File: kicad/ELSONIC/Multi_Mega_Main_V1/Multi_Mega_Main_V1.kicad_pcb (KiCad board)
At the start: 2 copper layers, 5 parts, among them U1 STM32G474METx, Y1 HC-49SMD

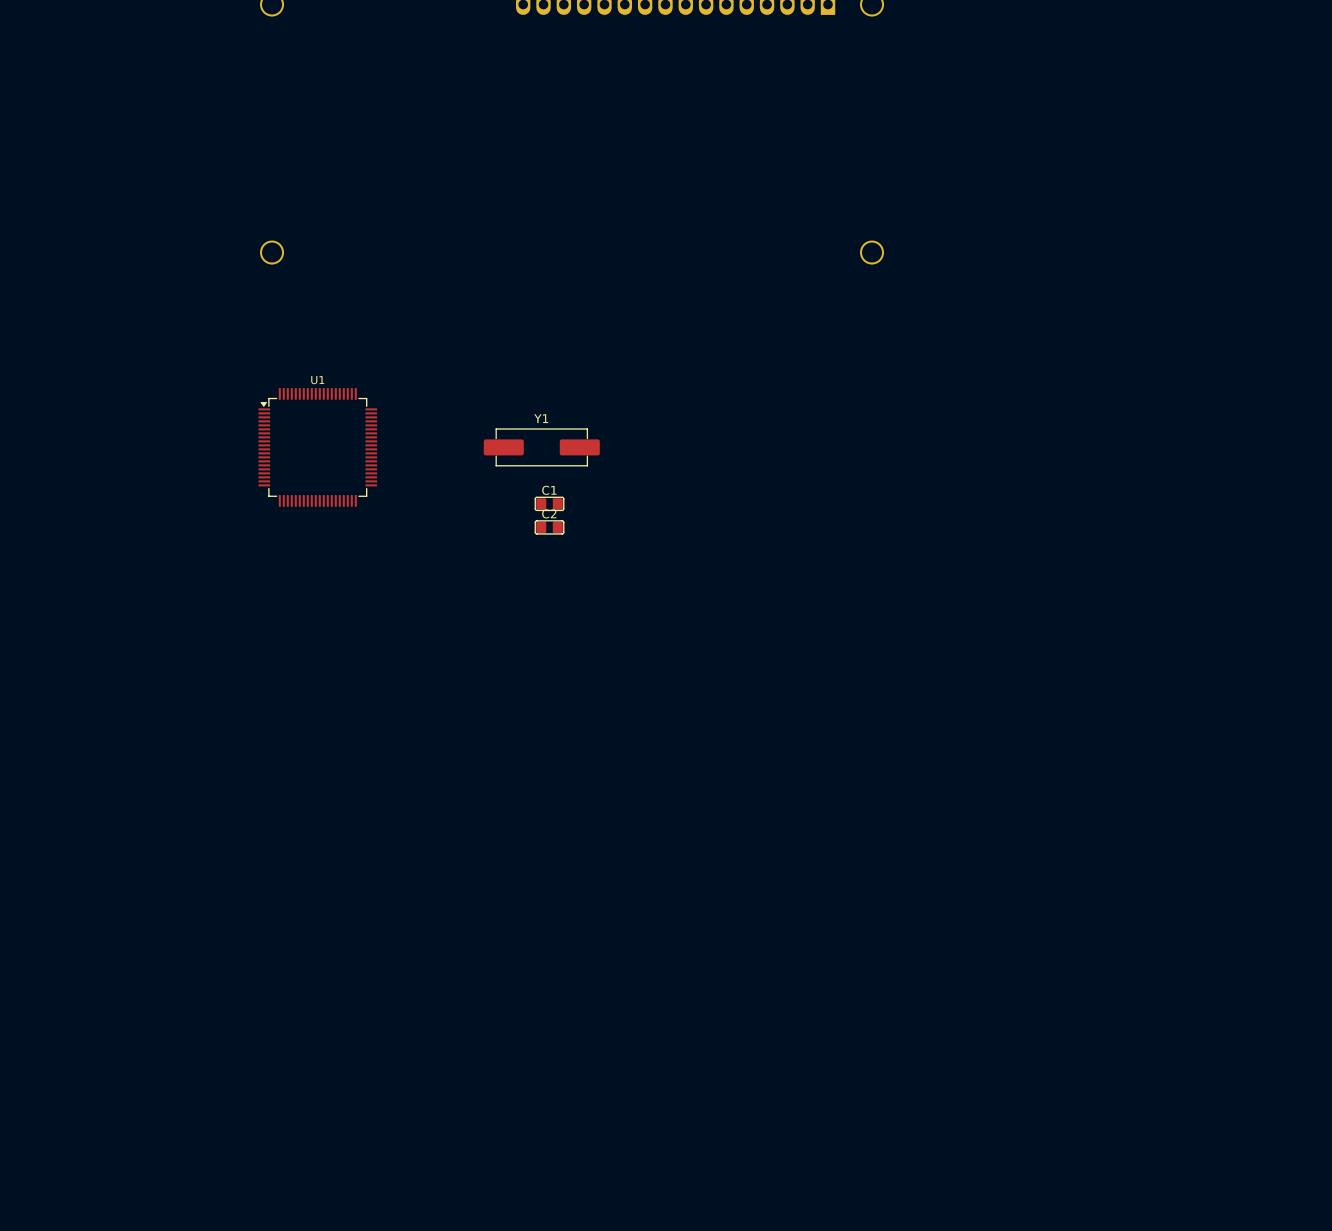
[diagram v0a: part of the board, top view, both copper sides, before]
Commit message: 회로도 구성 완료
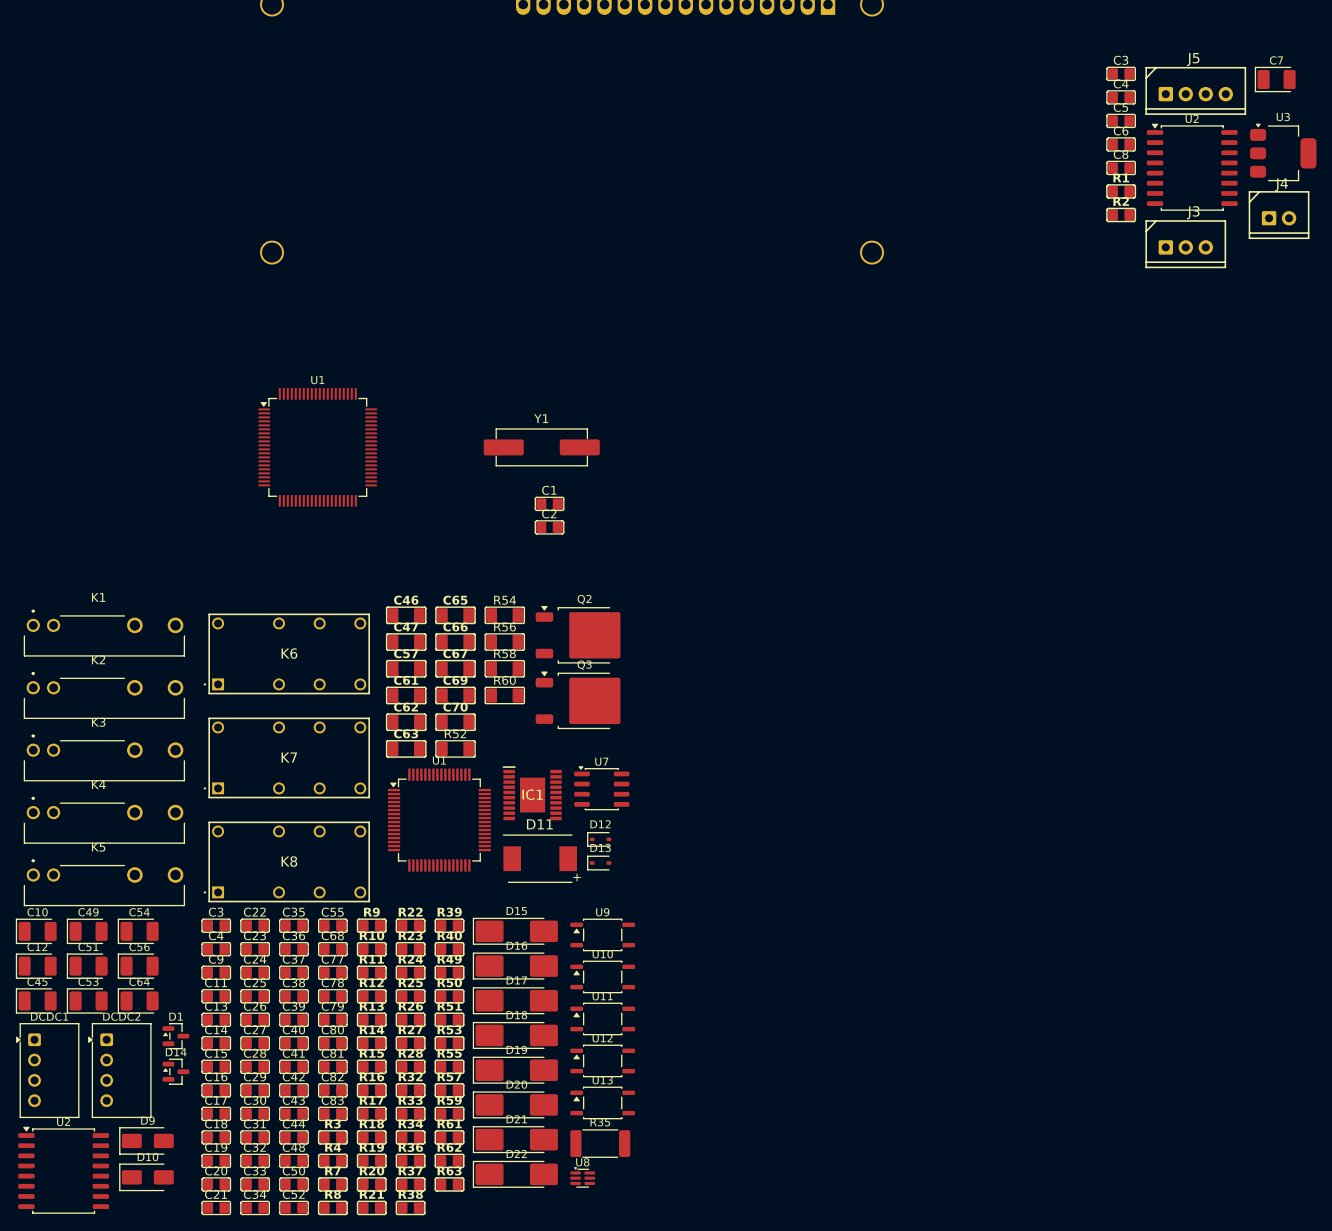
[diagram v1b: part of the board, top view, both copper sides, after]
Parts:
- added C10: 47UF50V, 04_MyFoot_Passive:CP_EIA-3528-21_Kemet-B_HandSolder, F.Cu at (46.0, 157.5)
- added C11: CL104K, 04_MyFoot_Passive:C_2012Metric, F.Cu at (68.3, 165.6)
- added C12: 10UF25V, 04_MyFoot_Passive:CP_EIA-3528-21_Kemet-B_HandSolder, F.Cu at (46.0, 161.8)
- added C13: CL104K, 04_MyFoot_Passive:C_2012Metric, F.Cu at (68.3, 168.6)
- added C14: CL475K, 04_MyFoot_Passive:C_2012Metric, F.Cu at (68.3, 171.5)
- added C15: CL104K, 04_MyFoot_Passive:C_2012Metric, F.Cu at (68.3, 174.4)
- added C16: CL104K, 04_MyFoot_Passive:C_2012Metric, F.Cu at (68.3, 177.4)
- added C17: CL105K, 04_MyFoot_Passive:C_2012Metric, F.Cu at (68.3, 180.3)
- added C18: CL104K, 04_MyFoot_Passive:C_2012Metric, F.Cu at (68.3, 183.2)
- added C19: CL104K, 04_MyFoot_Passive:C_2012Metric, F.Cu at (68.3, 186.2)
- added C20: CL104K, 04_MyFoot_Passive:C_2012Metric, F.Cu at (68.3, 189.1)
- added C21: CG101J, 04_MyFoot_Passive:C_2012Metric, F.Cu at (68.3, 192.1)
- added C22: CL104K, 04_MyFoot_Passive:C_2012Metric, F.Cu at (73.2, 156.8)
- added C23: CL104K, 04_MyFoot_Passive:C_2012Metric, F.Cu at (73.2, 159.7)
- added C24: CL104K, 04_MyFoot_Passive:C_2012Metric, F.Cu at (73.2, 162.7)
- added C25: CL104K, 04_MyFoot_Passive:C_2012Metric, F.Cu at (73.2, 165.6)
- added C26: CL104K, 04_MyFoot_Passive:C_2012Metric, F.Cu at (73.2, 168.6)
- added C27: CL104K, 04_MyFoot_Passive:C_2012Metric, F.Cu at (73.2, 171.5)
- added C28: CL106K, 04_MyFoot_Passive:C_2012Metric, F.Cu at (73.2, 174.4)
- added C29: CL104K, 04_MyFoot_Passive:C_2012Metric, F.Cu at (73.2, 177.4)
- added C3: CL104K, 04_MyFoot_Passive:C_2012Metric, F.Cu at (68.3, 156.8)
- added C3: CG220J, 04_MyFoot_Passive:C_2012Metric, F.Cu at (181.4, 50.3)
- added C30: CL475K, 04_MyFoot_Passive:C_2012Metric, F.Cu at (73.2, 180.3)
- added C31: CL104K, 04_MyFoot_Passive:C_2012Metric, F.Cu at (73.2, 183.2)
- added C32: CL104K, 04_MyFoot_Passive:C_2012Metric, F.Cu at (73.2, 186.2)
- added C33: CL105K, 04_MyFoot_Passive:C_2012Metric, F.Cu at (73.2, 189.1)
- added C34: CL104K, 04_MyFoot_Passive:C_2012Metric, F.Cu at (73.2, 192.1)
- added C35: B472K, 04_MyFoot_Passive:C_2012Metric, F.Cu at (78.0, 156.8)
- added C36: B472K, 04_MyFoot_Passive:C_2012Metric, F.Cu at (78.0, 159.7)
- added C37: CL104K, 04_MyFoot_Passive:C_2012Metric, F.Cu at (78.0, 162.7)
- added C38: CL104K, 04_MyFoot_Passive:C_2012Metric, F.Cu at (78.0, 165.6)
- added C39: CL104K, 04_MyFoot_Passive:C_2012Metric, F.Cu at (78.0, 168.6)
- added C4: CG220J, 04_MyFoot_Passive:C_2012Metric, F.Cu at (181.4, 53.2)
- added C4: CL475K, 04_MyFoot_Passive:C_2012Metric, F.Cu at (68.3, 159.7)
- added C40: CL104K, 04_MyFoot_Passive:C_2012Metric, F.Cu at (78.0, 171.5)
- added C41: CL104K, 04_MyFoot_Passive:C_2012Metric, F.Cu at (78.0, 174.4)
- added C42: CG220J, 04_MyFoot_Passive:C_2012Metric, F.Cu at (78.0, 177.4)
- added C43: CG220J, 04_MyFoot_Passive:C_2012Metric, F.Cu at (78.0, 180.3)
- added C44: CL104K, 04_MyFoot_Passive:C_2012Metric, F.Cu at (78.0, 183.2)
- added C45: TAJB106K, 04_MyFoot_Passive:CP_EIA-3528-21_Kemet-B_HandSolder, F.Cu at (46.0, 166.2)
- added C46: 225J100V, 04_MyFoot_Passive:C_3216Metric, F.Cu at (92.1, 118.0)
- added C47: 225J100V, 04_MyFoot_Passive:C_3216Metric, F.Cu at (92.1, 121.3)
- added C48: CL104K, 04_MyFoot_Passive:C_2012Metric, F.Cu at (78.0, 186.2)
- added C49: 47UF50V, 04_MyFoot_Passive:CP_EIA-3528-21_Kemet-B_HandSolder, F.Cu at (52.4, 157.5)
- added C5: CL104K, 04_MyFoot_Passive:C_2012Metric, F.Cu at (181.4, 56.2)
- added C50: CL104K, 04_MyFoot_Passive:C_2012Metric, F.Cu at (78.0, 189.1)
- added C51: 10UF25V, 04_MyFoot_Passive:CP_EIA-3528-21_Kemet-B_HandSolder, F.Cu at (52.4, 161.8)
- added C52: 104KC100V, 04_MyFoot_Passive:C_2012Metric, F.Cu at (78.0, 192.1)
- added C53: 10UF100V, 04_MyFoot_Passive:CP_EIA-3528-21_Kemet-B_HandSolder, F.Cu at (52.4, 166.2)
- added C54: 1000UF63V, 04_MyFoot_Passive:CP_EIA-3528-21_Kemet-B_HandSolder, F.Cu at (58.7, 157.5)
- added C55: CL104K, 04_MyFoot_Passive:C_2012Metric, F.Cu at (82.9, 156.8)
- added C56: TAJB106K, 04_MyFoot_Passive:CP_EIA-3528-21_Kemet-B_HandSolder, F.Cu at (58.7, 161.8)
- added C57: 105J100V, 04_MyFoot_Passive:C_3216Metric, F.Cu at (92.1, 124.7)
- added C6: CL104K, 04_MyFoot_Passive:C_2012Metric, F.Cu at (181.4, 59.1)
- added C61: 102J100V, 04_MyFoot_Passive:C_3216Metric, F.Cu at (92.1, 128.0)
- added C62: 223J100V, 04_MyFoot_Passive:C_3216Metric, F.Cu at (92.1, 131.3)
- added C63: 330J100V, 04_MyFoot_Passive:C_3216Metric, F.Cu at (92.1, 134.7)
- added C64: 220UF50V, 04_MyFoot_Passive:CP_EIA-3528-21_Kemet-B_HandSolder, F.Cu at (58.7, 166.2)
- added C65: 330J100V, 04_MyFoot_Passive:C_3216Metric, F.Cu at (98.2, 118.0)
- added C66: 103J100V, 04_MyFoot_Passive:C_3216Metric, F.Cu at (98.2, 121.3)
- added C67: 226J50V, 04_MyFoot_Passive:C_3216Metric, F.Cu at (98.2, 124.7)
- added C68: CL104K, 04_MyFoot_Passive:C_2012Metric, F.Cu at (82.9, 159.7)
- added C69: 103J100V, 04_MyFoot_Passive:C_3216Metric, F.Cu at (98.2, 128.0)
- added C7: TAJB106K, 04_MyFoot_Passive:CP_EIA-3528-21_Kemet-B_HandSolder, F.Cu at (200.9, 51.0)
- added C70: 101J100V, 04_MyFoot_Passive:C_3216Metric, F.Cu at (98.2, 131.3)
- added C77: B472K, 04_MyFoot_Passive:C_2012Metric, F.Cu at (82.9, 162.7)
- added C78: B472K, 04_MyFoot_Passive:C_2012Metric, F.Cu at (82.9, 165.6)
- added C79: B472K, 04_MyFoot_Passive:C_2012Metric, F.Cu at (82.9, 168.6)
- added C8: CL106K, 04_MyFoot_Passive:C_2012Metric, F.Cu at (181.4, 62.1)
- added C80: CL106K, 04_MyFoot_Passive:C_2012Metric, F.Cu at (82.9, 171.5)
- added C81: CL104K, 04_MyFoot_Passive:C_2012Metric, F.Cu at (82.9, 174.4)
- added C82: CL106K, 04_MyFoot_Passive:C_2012Metric, F.Cu at (82.9, 177.4)
- added C83: CL104K, 04_MyFoot_Passive:C_2012Metric, F.Cu at (82.9, 180.3)
- added C9: CL104K, 04_MyFoot_Passive:C_2012Metric, F.Cu at (68.3, 162.7)
- added D1: BAV99, Package_TO_SOT_SMD:SOT-23, F.Cu at (63.3, 170.6)
- added D10: SS24, Diode_SMD:D_SMA, F.Cu at (59.8, 188.2)
- added D11: B3100-13-F, 03_MyFoot_Active:B3100_13_F, F.Cu at (108.8, 148.4)
- added D12: BAT54WS, Diode_SMD:D_SOD-323, F.Cu at (116.3, 146.0)
- added D13: BAT54WS, Diode_SMD:D_SOD-323, F.Cu at (116.3, 149.0)
- added D14: SM712_SOT23, Package_TO_SOT_SMD:SOT-23, F.Cu at (63.3, 175.0)
- added D15: LL4148, 03_MyFoot_Active:D_MELF_Hand, F.Cu at (105.9, 157.5)
- added D16: LL4148, 03_MyFoot_Active:D_MELF_Hand, F.Cu at (105.9, 161.8)
- added D17: LL4148, 03_MyFoot_Active:D_MELF_Hand, F.Cu at (105.9, 166.2)
- added D18: LL4148, 03_MyFoot_Active:D_MELF_Hand, F.Cu at (105.9, 170.5)
- added D19: LL4148, 03_MyFoot_Active:D_MELF_Hand, F.Cu at (105.9, 174.8)
- added D20: LL4148, 03_MyFoot_Active:D_MELF_Hand, F.Cu at (105.9, 179.2)
- added D21: LL4148, 03_MyFoot_Active:D_MELF_Hand, F.Cu at (105.9, 183.5)
- added D22: LL4148, 03_MyFoot_Active:D_MELF_Hand, F.Cu at (105.9, 187.9)
- added D9: SS24, Diode_SMD:D_SMA, F.Cu at (59.8, 183.7)
- added DCDC1: MUS2415N, Converter_DCDC:Converter_DCDC_TRACO_TME_24xxS_Single_THT, F.Cu at (45.6, 171.0)
- added DCDC2: MUS2415N, Converter_DCDC:Converter_DCDC_TRACO_TME_24xxS_Single_THT, F.Cu at (54.6, 171.0)
- added IC1: LM5005MHX_NOPB, 01_MyFoot_ICs:SOP65P640X110-21N, F.Cu at (107.9, 140.5)
- added J3: SMW250-03P, 02_MyFoot_Connectors:SMW250_03P, F.Cu at (189.5, 72.0)
- added J4: SMW250-02P, 02_MyFoot_Connectors:SMW250_02P, F.Cu at (201.2, 68.4)
- added J5: SMW250-04P, 02_MyFoot_Connectors:SMW250_04P, F.Cu at (190.8, 52.8)
- added K1: PA1A_5V, 06_MyFoot_Mechanical:PA1A5V, F.Cu at (45.4, 119.2)
- added K2: PA1A_5V, 06_MyFoot_Mechanical:PA1A5V, F.Cu at (45.4, 127.0)
- added K3: PA1A_5V, 06_MyFoot_Mechanical:PA1A5V, F.Cu at (45.4, 134.8)
- added K4: PA1A_5V, 06_MyFoot_Mechanical:PA1A5V, F.Cu at (45.4, 142.7)
- added K5: PA1A_5V, 06_MyFoot_Mechanical:PA1A5V, F.Cu at (45.4, 150.4)
- added K6: G6A274, 06_MyFoot_Mechanical:G6A274PST15USDC12, F.Cu at (68.5, 126.6)
- added K7: G6A274, 06_MyFoot_Mechanical:G6A274PST15USDC12, F.Cu at (68.5, 139.6)
- added K8: G6A274, 06_MyFoot_Mechanical:G6A274PST15USDC12, F.Cu at (68.5, 152.6)
- added Q2: STD25N10F7, Package_TO_SOT_SMD:TO-252-2, F.Cu at (114.4, 120.5)
- added Q3: STD25N10F7, Package_TO_SOT_SMD:TO-252-2, F.Cu at (114.4, 128.7)
- added R1: FR-0747RL, 04_MyFoot_Passive:R_2012Metric, F.Cu at (181.4, 65.0)
- added R10: W8-J0561, 04_MyFoot_Passive:R_2012Metric, F.Cu at (87.7, 159.7)
- added R11: W8-J0561, 04_MyFoot_Passive:R_2012Metric, F.Cu at (87.7, 162.7)
- added R12: W8-J0561, 04_MyFoot_Passive:R_2012Metric, F.Cu at (87.7, 165.6)
- added R13: W8-J0561, 04_MyFoot_Passive:R_2012Metric, F.Cu at (87.7, 168.6)
- added R14: W8-J0103, 04_MyFoot_Passive:R_2012Metric, F.Cu at (87.7, 171.5)
- added R15: W8-J0103, 04_MyFoot_Passive:R_2012Metric, F.Cu at (87.7, 174.4)
- added R16: W8-J0103, 04_MyFoot_Passive:R_2012Metric, F.Cu at (87.7, 177.4)
- added R17: W8-J0103, 04_MyFoot_Passive:R_2012Metric, F.Cu at (87.7, 180.3)
- added R18: W8-J0103, 04_MyFoot_Passive:R_2012Metric, F.Cu at (87.7, 183.2)
- added R19: W4-J0220, 04_MyFoot_Passive:R_2012Metric, F.Cu at (87.7, 186.2)
- added R2: FR-0747RL, 04_MyFoot_Passive:R_2012Metric, F.Cu at (181.4, 68.0)
- added R20: W8-J0103, 04_MyFoot_Passive:R_2012Metric, F.Cu at (87.7, 189.1)
- added R21: W8-J0104, 04_MyFoot_Passive:R_2012Metric, F.Cu at (87.7, 192.1)
- added R22: W4-J0103, 04_MyFoot_Passive:R_2012Metric, F.Cu at (92.6, 156.8)
- added R23: 1W-4.7, 04_MyFoot_Passive:R_2012Metric, F.Cu at (92.6, 159.7)
- added R24: 1W-4.7, 04_MyFoot_Passive:R_2012Metric, F.Cu at (92.6, 162.7)
- added R25: W4-J0103, 04_MyFoot_Passive:R_2012Metric, F.Cu at (92.6, 165.6)
- added R26: W4-J0334, 04_MyFoot_Passive:R_2012Metric, F.Cu at (92.6, 168.6)
- added R27: W4-F4992, 04_MyFoot_Passive:R_2012Metric, F.Cu at (92.6, 171.5)
- added R28: W4-J0333, 04_MyFoot_Passive:R_2012Metric, F.Cu at (92.6, 174.4)
- added R3: W8-J0103, 04_MyFoot_Passive:R_2012Metric, F.Cu at (82.9, 183.2)
- added R32: W4-F1102, 04_MyFoot_Passive:R_2012Metric, F.Cu at (92.6, 177.4)
- added R33: W4-F1501, 04_MyFoot_Passive:R_2012Metric, F.Cu at (92.6, 180.3)
- added R34: W4-F2701, 04_MyFoot_Passive:R_2012Metric, F.Cu at (92.6, 183.2)
- added R35: 1W-F100, Resistor_SMD:R_2512_6332Metric_Pad1.40x3.35mm_HandSolder, F.Cu at (116.3, 184.0)
- added R36: W4-J0100, 04_MyFoot_Passive:R_2012Metric, F.Cu at (92.6, 186.2)
- added R37: W4-J0123, 04_MyFoot_Passive:R_2012Metric, F.Cu at (92.6, 189.1)
- added R38: W4-J0223, 04_MyFoot_Passive:R_2012Metric, F.Cu at (92.6, 192.1)
- added R39: W4-F1102, 04_MyFoot_Passive:R_2012Metric, F.Cu at (97.5, 156.8)
- added R4: W4-J0470, 04_MyFoot_Passive:R_2012Metric, F.Cu at (82.9, 186.2)
- added R40: W4-F1501, 04_MyFoot_Passive:R_2012Metric, F.Cu at (97.5, 159.7)
- added R49: W8-J0431, 04_MyFoot_Passive:R_2012Metric, F.Cu at (97.5, 162.7)
- added R50: W8-J0431, 04_MyFoot_Passive:R_2012Metric, F.Cu at (97.5, 165.6)
- added R51: W4-J0121, 04_MyFoot_Passive:R_2012Metric, F.Cu at (97.5, 168.6)
- added R52: W4-J0472, 04_MyFoot_Passive:R_3216Metric, F.Cu at (98.2, 134.7)
- added R53: W8-J0103, 04_MyFoot_Passive:R_2012Metric, F.Cu at (97.5, 171.5)
- added R54: W4-J0472, 04_MyFoot_Passive:R_3216Metric, F.Cu at (104.4, 118.0)
- added R55: W8-J0103, 04_MyFoot_Passive:R_2012Metric, F.Cu at (97.5, 174.4)
- added R56: W4-J0472, 04_MyFoot_Passive:R_3216Metric, F.Cu at (104.4, 121.3)
- added R57: W8-J0103, 04_MyFoot_Passive:R_2012Metric, F.Cu at (97.5, 177.4)
- added R58: W4-J0472, 04_MyFoot_Passive:R_3216Metric, F.Cu at (104.4, 124.7)
- added R59: W8-J0103, 04_MyFoot_Passive:R_2012Metric, F.Cu at (97.5, 180.3)
- added R60: W4-J0472, 04_MyFoot_Passive:R_3216Metric, F.Cu at (104.4, 128.0)
- added R61: W8-J0103, 04_MyFoot_Passive:R_2012Metric, F.Cu at (97.5, 183.2)
- added R62: FR-0733RL, 04_MyFoot_Passive:R_2012Metric, F.Cu at (97.5, 186.2)
- added R63: W8-J0103, 04_MyFoot_Passive:R_2012Metric, F.Cu at (97.5, 189.1)
- added R7: W8-J0103, 04_MyFoot_Passive:R_2012Metric, F.Cu at (82.9, 189.1)
- added R8: W8-J0561, 04_MyFoot_Passive:R_2012Metric, F.Cu at (82.9, 192.1)
- added R9: W8-J0561, 04_MyFoot_Passive:R_2012Metric, F.Cu at (87.7, 156.8)
- added U1: STM32G474RBT6, Package_QFP:LQFP-64_10x10mm_P0.5mm, F.Cu at (96.2, 143.6)
- added U10: TLP185, 01_MyFoot_ICs:SOIC-4_4.55x3.7mm_P2.54mm, F.Cu at (116.6, 163.2)
- added U11: TLP185, 01_MyFoot_ICs:SOIC-4_4.55x3.7mm_P2.54mm, F.Cu at (116.6, 168.4)
- added U12: TLP185, 01_MyFoot_ICs:SOIC-4_4.55x3.7mm_P2.54mm, F.Cu at (116.6, 173.7)
- added U13: TLP185, 01_MyFoot_ICs:SOIC-4_4.55x3.7mm_P2.54mm, F.Cu at (116.6, 178.9)
- added U2: UCC21520DW, Package_SO:SOIC-16W_7.5x10.3mm_P1.27mm, F.Cu at (49.2, 187.5)
- added U2: UCC21520DW, Package_SO:SOIC-16W_7.5x10.3mm_P1.27mm, F.Cu at (190.3, 62.1)
- added U3: AMS1117-3.3, Package_TO_SOT_SMD:SOT-223-3_TabPin2, F.Cu at (201.7, 60.2)
- added U7: MAX3485, Package_SO:SOIC-8_3.9x4.9mm_P1.27mm, F.Cu at (116.5, 139.7)
- added U8: INA190A4, Package_TO_SOT_SMD:SOT-363_SC-70-6, F.Cu at (114.1, 188.3)
- added U9: TLP185, 01_MyFoot_ICs:SOIC-4_4.55x3.7mm_P2.54mm, F.Cu at (116.6, 157.9)
- LCD1: renamed from DS1; value WC1602A -> LC1602A
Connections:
- LCD1 pad 1: unconnected-(DS1-VSS-Pad1) -> GND
- LCD1 pad 11: unconnected-(DS1-D4-Pad11) -> Net-(LCD1-D4)
- LCD1 pad 12: unconnected-(DS1-D5-Pad12) -> Net-(LCD1-D5)
- LCD1 pad 13: unconnected-(DS1-D6-Pad13) -> Net-(LCD1-D6)
- LCD1 pad 14: unconnected-(DS1-D7-Pad14) -> Net-(LCD1-D7)
- LCD1 pad 15: unconnected-(DS1-LED(+)-Pad15) -> Net-(LCD1-LED(+))
- LCD1 pad 16: unconnected-(DS1-LED(-)-Pad16) -> GND
- LCD1 pad 2: unconnected-(DS1-VDD-Pad2) -> +5V
- LCD1 pad 3: unconnected-(DS1-VO-Pad3) -> Net-(LCD1-VO)
- LCD1 pad 4: unconnected-(DS1-RS-Pad4) -> Net-(LCD1-RS)
- LCD1 pad 5: unconnected-(DS1-R/W-Pad5) -> GND
- LCD1 pad 6: unconnected-(DS1-E-Pad6) -> Net-(LCD1-E)
- U1 pad 56: unconnected-(U1-PA8-Pad56) -> Net-(U1-PA8)
- U1 pad 57: unconnected-(U1-PA9-Pad57) -> Net-(U1-PA9)

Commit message: chore: KiCad 아트웍 및 라이브러리 변경 반영
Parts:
- removed the U1 at (81.0, 97.0)
- added D23: LL4148, 03_MyFoot_Active:D_MELF_Hand, F.Cu at (111.5, -91.5)
- added K9: G6A274, 06_MyFoot_Mechanical:G6A274PST15USDC12, F.Cu at (108.2, -96.4)
- moved C1 301.6 mm to (110.0, -197.6)
- moved C10 301.6 mm to (46.0, -144.1)
- moved C11 301.6 mm to (68.3, -136.0)
- moved C12 301.6 mm to (46.0, -139.8)
- moved C13 301.6 mm to (68.3, -133.1)
- moved C14 301.6 mm to (68.3, -130.1)
- moved C15 301.6 mm to (68.3, -127.2)
- moved C16 301.6 mm to (68.3, -124.2)
- moved C17 301.6 mm to (68.3, -121.3)
- moved C18 301.6 mm to (68.3, -118.4)
- moved C19 301.6 mm to (68.3, -115.4)
- moved C2 301.6 mm to (110.0, -194.6)
- moved C20 301.6 mm to (68.3, -112.5)
- moved C21 301.6 mm to (68.3, -109.5)
- moved C22 301.6 mm to (73.2, -144.8)
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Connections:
- net /LC_RELAY_OUT renamed Net-(K8-NC1)
